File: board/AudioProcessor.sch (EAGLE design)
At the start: 43 parts, among them IC1 ATTINY24/44/84-SSU, IC2 LP2951, IC3 LP2951, IC4 TDA7439DS, J1 PINHD-1X3-JST-PH, J2 PINHD-1X3-JST-PH, J3 PINHD-1X3-JST-PH, J4 PINHD-1X3-JST-PH, J5 PINHD-1X3-JST-PH, J6 PINHD-1X6-JST-PH

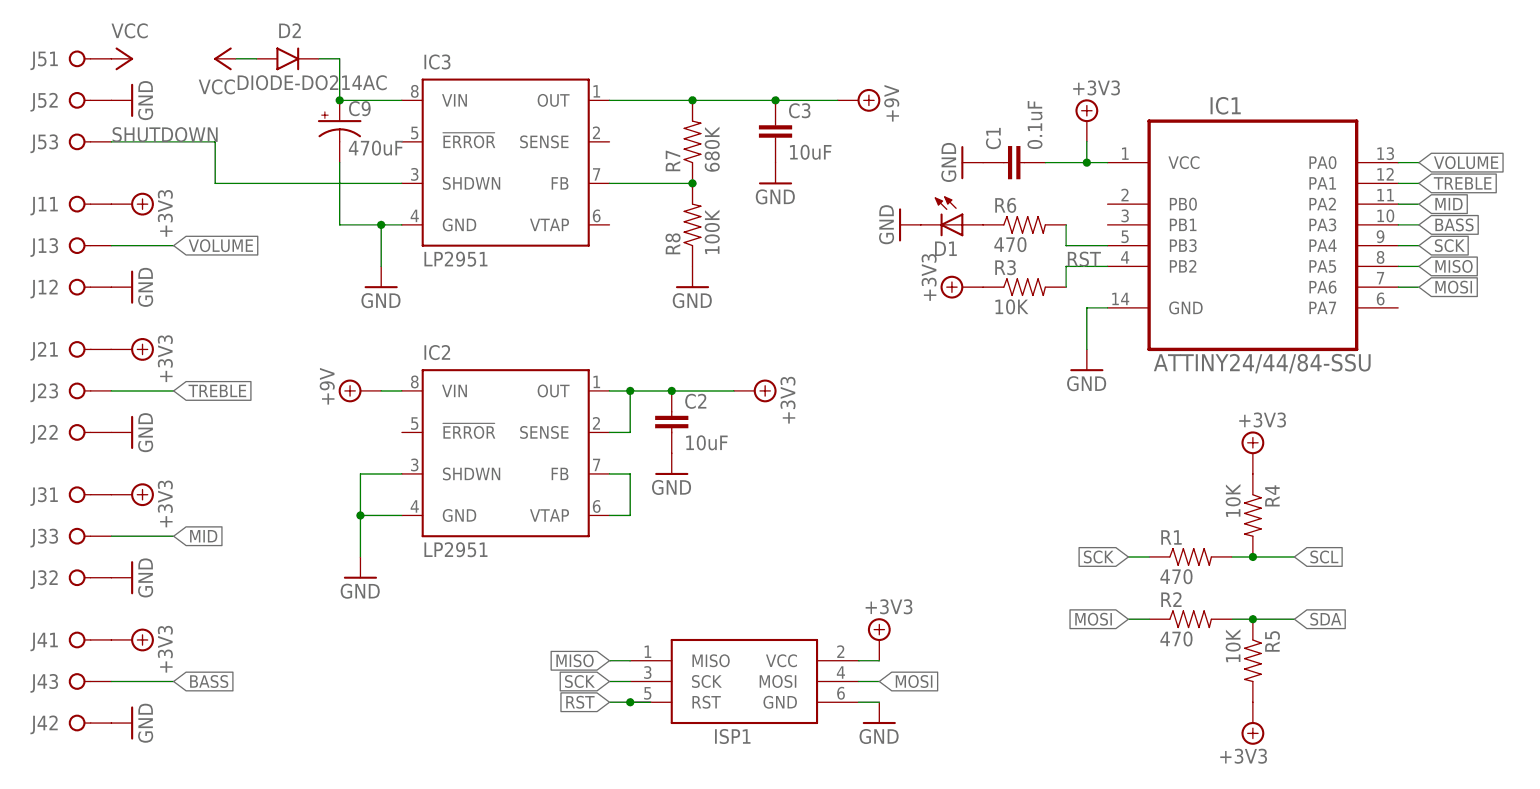
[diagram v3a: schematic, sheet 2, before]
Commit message: Update with library changes and tune for Macrofab house parts
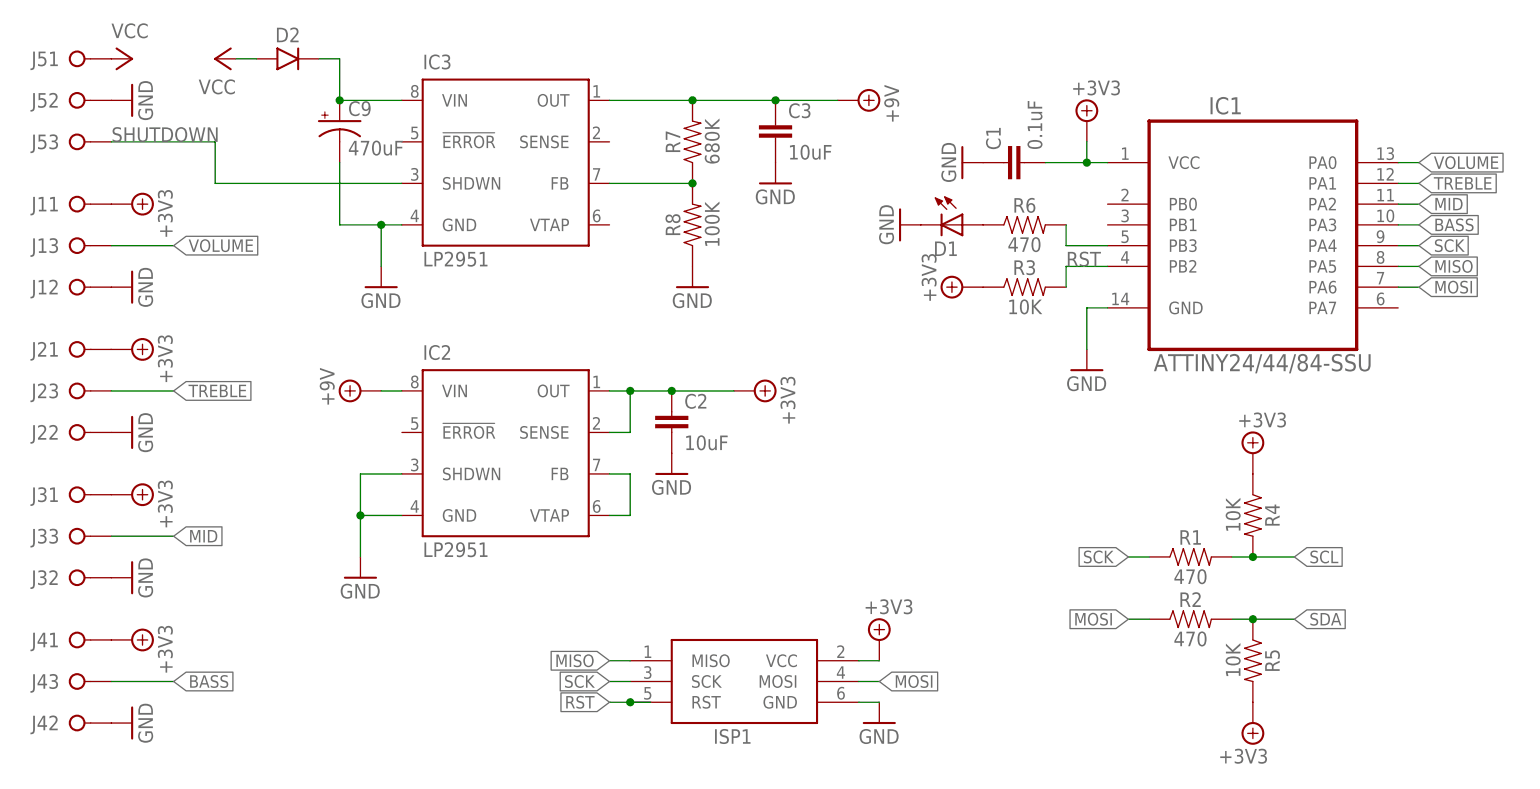
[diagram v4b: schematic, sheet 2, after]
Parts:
- C1, C5: device SaintGimp:CAPACITOR-0805 -> SaintGimp:CAPACITOR-0603
- C9: device SaintGimp:CAP-POL- -> SaintGimp:CAPACITOR-POLARIZED-3.5-8
- D2: value DIODE-DO214AC -> (none)
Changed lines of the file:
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@@
 <parts>
 <part name="IC4" library="SaintGimp" deviceset="TDA7439DS" device=""/>
-<part name="C10" library="SaintGimp" deviceset="CAPACITOR-*" device="5MM" value="5.6nF"/>
+<part name="C10" library="SaintGimp" deviceset="CAPACITOR" device="-5MM" value="5.6nF"/>
 <part name="GND3" library="SaintGimp" deviceset="GND" device=""/>
 <part name="GND9" library="SaintGimp" deviceset="GND" device=""/>
-<part name="C18" library="SaintGimp" deviceset="CAPACITOR-*" device="5MM" value="18nF"/>
-<part name="C17" library="SaintGimp" deviceset="CAPACITOR-*" device="5MM" value="22nF"/>
+<part name="C18" library="SaintGimp" deviceset="CAPACITOR" device="-5MM" value="18nF"/>
+<part name="C17" library="SaintGimp" deviceset="CAPACITOR" device="-5MM" value="22nF"/>
 <part name="R10" library="SaintGimp" deviceset="RESISTOR-*" device="0805" value="2.7K"/>
-<part name="C15" library="SaintGimp" deviceset="CAPACITOR-*" device="5MM" value="100nF"/>
-<part name="C16" library="SaintGimp" deviceset="CAPACITOR-*" device="5MM" value="100nF"/>
+<part name="C15" library="SaintGimp" deviceset="CAPACITOR" device="-5MM" value="100nF"/>
+<part name="C16" library="SaintGimp" deviceset="CAPACITOR" device="-5MM" value="100nF"/>
 <part name="R12" library="SaintGimp" deviceset="RESISTOR-*" device="0805" value="5.6K"/>
 <part name="GND5" library="SaintGimp" deviceset="GND" device=""/>
 <part name="GND7" library="SaintGimp" deviceset="GND" device=""/>
-<part name="C8" library="SaintGimp" deviceset="CAPACITOR-*" device="5MM" value="5.6nF"/>
+<part name="C8" library="SaintGimp" deviceset="CAPACITOR" device="-5MM" value="5.6nF"/>
 <part name="GND4" library="SaintGimp" deviceset="GND" device=""/>
-<part name="C11" library="SaintGimp" deviceset="CAPACITOR-*" device="5MM" value="18nF"/>
-<part name="C12" library="SaintGimp" deviceset="CAPACITOR-*" device="5MM" value="22nF"/>
+<part name="C11" library="SaintGimp" deviceset="CAPACITOR" device="-5MM" value="18nF"/>
+<part name="C12" library="SaintGimp" deviceset="CAPACITOR" device="-5MM" value="22nF"/>
 <part name="R11" library="SaintGimp" deviceset="RESISTOR-*" device="0805" value="2.7K"/>
-<part name="C13" library="SaintGimp" deviceset="CAPACITOR-*" device="5MM" value="100nF"/>
-<part name="C14" library="SaintGimp" deviceset="CAPACITOR-*" device="5MM" value="100nF"/>
+<part name="C13" library="SaintGimp" deviceset="CAPACITOR" device="-5MM" value="100nF"/>
+<part name="C14" library="SaintGimp" deviceset="CAPACITOR" device="-5MM" value="100nF"/>
 <part name="R9" library="SaintGimp" deviceset="RESISTOR-*" device="0805" value="5.6K"/>
 <part name="GND8" library="SaintGimp" deviceset="GND" device=""/>
 <part name="GND6" library="SaintGimp" deviceset="GND" device=""/>
-<part name="C6" library="SaintGimp" deviceset="CAPACITOR-*" device="1206" value="10uF"/>
+<part name="C6" library="SaintGimp" deviceset="CAPACITOR" device="-1206" value="10uF"/>
 <part name="GND11" library="SaintGimp" deviceset="GND" device=""/>
 <part name="IC1" library="SaintGimp" deviceset="ATTINY24/44/84" device="-SSU" value="ATTINY24/44/84-SSU"/>
@@
 <part name="GND26" library="SaintGimp" deviceset="GND" device=""/>
 <part name="P+9" library="SaintGimp" deviceset="VCC" device=""/>
-<part name="C3" library="SaintGimp" deviceset="CAPACITOR-*" device="1206" value="10uF"/>
+<part name="C3" library="SaintGimp" deviceset="CAPACITOR" device="-1206" value="10uF"/>
 <part name="GND23" library="SaintGimp" deviceset="GND" device=""/>
-<part name="C2" library="SaintGimp" deviceset="CAPACITOR-*" device="1206" value="10uF"/>
+<part name="C2" library="SaintGimp" deviceset="CAPACITOR" device="-1206" value="10uF"/>
 <part name="GND21" library="SaintGimp" deviceset="GND" device=""/>
-<part name="C5" library="SaintGimp" deviceset="CAPACITOR-*" device="0805" value="0.1uF"/>
+<part name="C5" library="SaintGimp" deviceset="CAPACITOR" device="-0603" value="0.1uF"/>
 <part name="GND10" library="SaintGimp" deviceset="GND" device=""/>
-<part name="C1" library="SaintGimp" deviceset="CAPACITOR-*" device="0805" value="0.1uF"/>
+<part name="C1" library="SaintGimp" deviceset="CAPACITOR" device="-0603" value="0.1uF"/>
 <part name="GND25" library="SaintGimp" deviceset="GND" device=""/>
 <part name="ISP1" library="SaintGimp" deviceset="ICSP-HEADER" device="-6"/>
@@
 <part name="P+10" library="SaintGimp" deviceset="+9V" device=""/>
 <part name="P+12" library="SaintGimp" deviceset="+9V" device=""/>
-<part name="C7" library="SaintGimp" deviceset="CAPACITOR-*" device="5MM" value="0.47uF"/>
-<part name="C4" library="SaintGimp" deviceset="CAPACITOR-*" device="5MM" value="0.47uF"/>
+<part name="C7" library="SaintGimp" deviceset="CAPACITOR" device="-5MM" value="0.47uF"/>
+<part name="C4" library="SaintGimp" deviceset="CAPACITOR" device="-5MM" value="0.47uF"/>
 <part name="R4" library="SaintGimp" deviceset="RESISTOR-*" device="0805" value="10K"/>
 <part name="R5" library="SaintGimp" deviceset="RESISTOR-*" device="0805" value="10K"/>
@@
 <part name="GND18" library="SaintGimp" deviceset="GND" device=""/>
 <part name="J5" library="SaintGimp" deviceset="PINHD-1X3" device="-JST-PH"/>
-<part name="C9" library="SaintGimp" deviceset="CAP-POL-*" device="" value="470uF"/>
+<part name="C9" library="SaintGimp" deviceset="CAPACITOR-POLARIZED" device="-3.5-8" value="470uF"/>
 <part name="R6" library="SaintGimp" deviceset="RESISTOR-*" device="0805" value="470"/>
 <part name="D1" library="SaintGimp" deviceset="LED-*" device="0805"/>
 <part name="GND12" library="SaintGimp" deviceset="GND" device=""/>
-<part name="D2" library="SaintGimp" deviceset="DIODE-*" device="DO214AC"/>
+<part name="D2" library="SaintGimp" deviceset="DIODE" device="-DO214AC"/>
 </parts>
 <sheets>

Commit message: Fix JST header orientation
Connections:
- removed net SHUTDOWN: IC3.SHDWN, J53.KL
- net +3V3: now also J13.KL, J23.KL, J33.KL, J43.KL; no longer J11.KL, J21.KL, J31.KL, J41.KL
- net BASS: now also J41.KL; no longer J43.KL
- net GND: now also IC3.SHDWN
- net L-IN-RAW: now also J61.KL; no longer J66.KL
- net L-OUT: now also J62.KL; no longer J65.KL
- net MID: now also J31.KL; no longer J33.KL
- net R-IN-RAW: now also J66.KL; no longer J61.KL
- net R-OUT: now also J65.KL; no longer J62.KL
- net TREBLE: now also J21.KL; no longer J23.KL
- net VCC: now also J53.KL; no longer J51.KL
- net VOLUME: now also J11.KL; no longer J13.KL
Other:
- moved on the sheet: J11, J13, J21, J23, J31, J33, J41, J43, J53, J61, J62, J65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
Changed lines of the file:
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@@
 <instance part="C7" gate="G$1" x="33.02" y="55.88" rot="R90"/>
 <instance part="C4" gate="G$1" x="33.02" y="35.56" rot="R90"/>
-<instance part="J6" gate="6" x="20.32" y="55.88"/>
-<instance part="J6" gate="5" x="119.38" y="40.64" rot="R180"/>
+<instance part="J6" gate="1" x="20.32" y="55.88"/>
+<instance part="J6" gate="2" x="119.38" y="40.64" rot="R180"/>
 <instance part="J6" gate="3" x="22.86" y="10.16"/>
 <instance part="J6" gate="4" x="22.86" y="5.08"/>
-<instance part="J6" gate="2" x="119.38" y="35.56" rot="R180"/>
-<instance part="J6" gate="1" x="20.32" y="35.56"/>
+<instance part="J6" gate="5" x="119.38" y="35.56" rot="R180"/>
+<instance part="J6" gate="6" x="20.32" y="35.56"/>
 <instance part="GND2" gate="1" x="30.48" y="5.08" rot="R90"/>
 <instance part="GND1" gate="1" x="30.48" y="10.16" rot="R90"/>
@@
 <pinref part="IC4" gate="G$1" pin="L-OUT"/>
 <wire x1="114.3" y1="40.64" x2="109.22" y2="40.64" width="0.1524" layer="91"/>
-<pinref part="J6" gate="5" pin="KL"/>
+<pinref part="J6" gate="2" pin="KL"/>
 </segment>
 </net>
@@
 <pinref part="IC4" gate="G$1" pin="R-OUT"/>
 <wire x1="109.22" y1="35.56" x2="114.3" y2="35.56" width="0.1524" layer="91"/>
-<pinref part="J6" gate="2" pin="KL"/>
+<pinref part="J6" gate="5" pin="KL"/>
 </segment>
 </net>
@@
 <segment>
 <pinref part="C7" gate="G$1" pin="1"/>
+<pinref part="J6" gate="1" pin="KL"/>
+<wire x1="25.4" y1="55.88" x2="27.94" y2="55.88" width="0.1524" layer="91"/>
+</segment>
+</net>
+<net name="R-IN-RAW" class="0">
+<segment>
+<pinref part="C4" gate="G$1" pin="1"/>
 <pinref part="J6" gate="6" pin="KL"/>
-<wire x1="25.4" y1="55.88" x2="27.94" y2="55.88" width="0.1524" layer="91"/>
-</segment>
-</net>
-<net name="R-IN-RAW" class="0">
-<segment>
-<pinref part="C4" gate="G$1" pin="1"/>
-<pinref part="J6" gate="1" pin="KL"/>
 <wire x1="25.4" y1="35.56" x2="27.94" y2="35.56" width="0.1524" layer="91"/>
 </segment>
@@
 <instance part="R3" gate="G$1" x="15.24" y="121.92"/>
 <instance part="P+14" gate="G$1" x="7.62" y="121.92" rot="R90"/>
-<instance part="J1" gate="1" x="-101.6" y="132.08"/>
-<instance part="J1" gate="3" x="-101.6" y="127"/>
+<instance part="J1" gate="3" x="-101.6" y="132.08"/>
+<instance part="J1" gate="1" x="-101.6" y="127"/>
 <instance part="J1" gate="2" x="-101.6" y="121.92"/>
-<instance part="J2" gate="1" x="-101.6" y="114.3"/>
-<instance part="J2" gate="3" x="-101.6" y="109.22"/>
+<instance part="J2" gate="3" x="-101.6" y="114.3"/>
+<instance part="J2" gate="1" x="-101.6" y="109.22"/>
 <instance part="J2" gate="2" x="-101.6" y="104.14"/>
-<instance part="J3" gate="1" x="-101.6" y="96.52"/>
-<instance part="J3" gate="3" x="-101.6" y="91.44"/>
+<instance part="J3" gate="3" x="-101.6" y="96.52"/>
+<instance part="J3" gate="1" x="-101.6" y="91.44"/>
 <instance part="J3" gate="2" x="-101.6" y="86.36"/>
-<instance part="J4" gate="1" x="-101.6" y="78.74"/>
-<instance part="J4" gate="3" x="-101.6" y="73.66"/>
+<instance part="J4" gate="3" x="-101.6" y="78.74"/>
+<instance part="J4" gate="1" x="-101.6" y="73.66"/>
 <instance part="J4" gate="2" x="-101.6" y="68.58"/>
 <instance part="P+5" gate="G$1" x="-93.98" y="132.08" rot="R270"/>
@@
 <instance part="P+4" gate="VCC" x="-93.98" y="149.86" rot="R270"/>
 <instance part="GND14" gate="1" x="-93.98" y="144.78" rot="R90"/>
-<instance part="J5" gate="1" x="-101.6" y="149.86"/>
+<instance part="J5" gate="3" x="-101.6" y="149.86"/>
 <instance part="J5" gate="2" x="-101.6" y="144.78"/>
-<instance part="J5" gate="3" x="-101.6" y="139.7"/>
 <instance part="C9" gate="G$1" x="-68.58" y="142.24"/>
 <instance part="R6" gate="G$1" x="15.24" y="129.54"/>
@@
 <junction x="-63.5" y="129.54"/>
 <pinref part="C9" gate="G$1" pin="-"/>
+<pinref part="IC3" gate="G$1" pin="SHDWN"/>
+<wire x1="-60.96" y1="134.62" x2="-63.5" y2="134.62" width="0.1524" layer="91"/>
+<wire x1="-63.5" y1="134.62" x2="-63.5" y2="129.54" width="0.1524" layer="91"/>
 </segment>
 <segment>
@@
 </segment>
 <segment>
-<pinref part="J1" gate="1" pin="KL"/>
+<pinref part="J1" gate="3" pin="KL"/>
 <pinref part="P+5" gate="G$1" pin="+3V3"/>
 </segment>
 <segment>
-<pinref part="J2" gate="1" pin="KL"/>
+<pinref part="J2" gate="3" pin="KL"/>
 <pinref part="P+6" gate="G$1" pin="+3V3"/>
 </segment>
 <segment>
-<pinref part="J3" gate="1" pin="KL"/>
+<pinref part="J3" gate="3" pin="KL"/>
 <pinref part="P+7" gate="G$1" pin="+3V3"/>
 </segment>
 <segment>
-<pinref part="J4" gate="1" pin="KL"/>
+<pinref part="J4" gate="3" pin="KL"/>
 <pinref part="P+8" gate="G$1" pin="+3V3"/>
 </segment>
@@
 <segment>
 <pinref part="P+4" gate="VCC" pin="VCC"/>
-<pinref part="J5" gate="1" pin="KL"/>
+<pinref part="J5" gate="3" pin="KL"/>
 </segment>
 <segment>
@@
 </segment>
 <segment>
-<pinref part="J1" gate="3" pin="KL"/>
+<pinref part="J1" gate="1" pin="KL"/>
 <wire x1="-96.52" y1="127" x2="-88.9" y2="127" width="0.1524" layer="91"/>
 <label x="-88.9" y="127" size="1.524" layer="95" xref="yes"/>
@@
 </segment>
 <segment>
-<pinref part="J2" gate="3" pin="KL"/>
+<pinref part="J2" gate="1" pin="KL"/>
 <wire x1="-96.52" y1="109.22" x2="-88.9" y2="109.22" width="0.1524" layer="91"/>
 <label x="-88.9" y="109.22" size="1.524" layer="95" xref="yes"/>
@@
 </segment>
 <segment>
-<pinref part="J3" gate="3" pin="KL"/>
+<pinref part="J3" gate="1" pin="KL"/>
 <wire x1="-96.52" y1="91.44" x2="-88.9" y2="91.44" width="0.1524" layer="91"/>
 <label x="-88.9" y="91.44" size="1.524" layer="95" xref="yes"/>
@@
 </segment>
 <segment>
-<pinref part="J4" gate="3" pin="KL"/>
+<pinref part="J4" gate="1" pin="KL"/>
 <wire x1="-96.52" y1="73.66" x2="-88.9" y2="73.66" width="0.1524" layer="91"/>
 <label x="-88.9" y="73.66" size="1.524" layer="95" xref="yes"/>
 </segment>
 </net>
-<net name="SHUTDOWN" class="0">
-<segment>
-<pinref part="IC3" gate="G$1" pin="SHDWN"/>
-<wire x1="-60.96" y1="134.62" x2="-83.82" y2="134.62" width="0.1524" layer="91"/>
-<wire x1="-83.82" y1="134.62" x2="-83.82" y2="139.7" width="0.1524" layer="91"/>
-<pinref part="J5" gate="3" pin="KL"/>
-<wire x1="-83.82" y1="139.7" x2="-96.52" y2="139.7" width="0.1524" layer="91"/>
-<label x="-96.52" y="139.7" size="1.778" layer="95"/>
-</segment>
-</net>

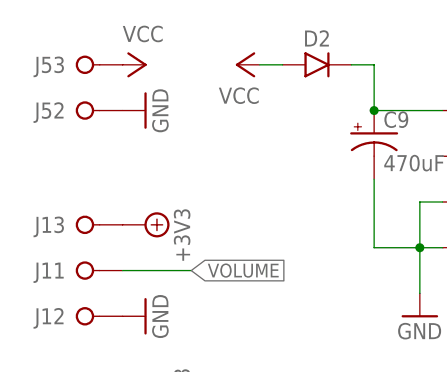
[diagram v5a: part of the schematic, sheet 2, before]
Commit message: Board updates for manufacturing
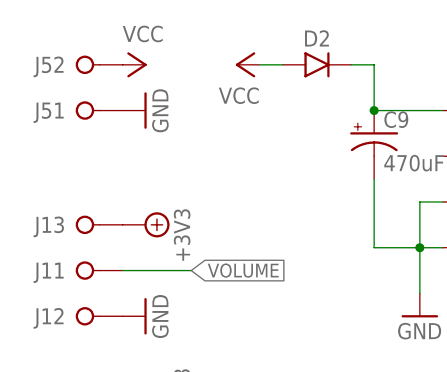
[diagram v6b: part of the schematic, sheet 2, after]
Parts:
- J5: value PINHD-1X3-JST-PH -> PINHD-1X2-JST-PH; device SaintGimp:PINHD-1X3-JST-PH -> SaintGimp:PINHD-1X2-JST-PH
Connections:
- net GND: now also J51.KL; no longer J52.KL
- net VCC: now also J52.KL; no longer J53.KL
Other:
- moved on the sheet: J52
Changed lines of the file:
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@@
 <part name="GND17" library="SaintGimp" deviceset="GND" device=""/>
 <part name="GND18" library="SaintGimp" deviceset="GND" device=""/>
-<part name="J5" library="SaintGimp" deviceset="PINHD-1X3" device="-JST-PH"/>
+<part name="J5" library="SaintGimp" deviceset="PINHD-1X2" device="-JST-PH"/>
 <part name="C9" library="SaintGimp" deviceset="CAPACITOR-POLARIZED" device="-3.5-8" value="470uF"/>
 <part name="R6" library="SaintGimp" deviceset="RESISTOR-*" device="0805" value="470"/>
@@
 <instance part="P+4" gate="VCC" x="-93.98" y="149.86" rot="R270"/>
 <instance part="GND14" gate="1" x="-93.98" y="144.78" rot="R90"/>
-<instance part="J5" gate="3" x="-101.6" y="149.86"/>
-<instance part="J5" gate="2" x="-101.6" y="144.78"/>
+<instance part="J5" gate="2" x="-101.6" y="149.86"/>
+<instance part="J5" gate="1" x="-101.6" y="144.78"/>
 <instance part="C9" gate="G$1" x="-68.58" y="142.24"/>
 <instance part="R6" gate="G$1" x="15.24" y="129.54"/>
@@
 <segment>
 <pinref part="GND14" gate="1" pin="GND"/>
-<pinref part="J5" gate="2" pin="KL"/>
+<pinref part="J5" gate="1" pin="KL"/>
 </segment>
 <segment>
@@
 <segment>
 <pinref part="P+4" gate="VCC" pin="VCC"/>
-<pinref part="J5" gate="3" pin="KL"/>
-</segment>
-<segment>
+<pinref part="J5" gate="2" pin="KL"/>
+</segment>
+<segment>
